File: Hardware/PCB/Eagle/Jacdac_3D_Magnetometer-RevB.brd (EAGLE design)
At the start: 25 x 25 mm, 31 parts, among them J2 SWD-ADAPTER-, J3 5V, J4 DATA, J5 GND, J6 GND, U1 STM32G030F6P6, U2 NCP114ASN330T1G, U3 TLV493D, U4 BAT54S,235

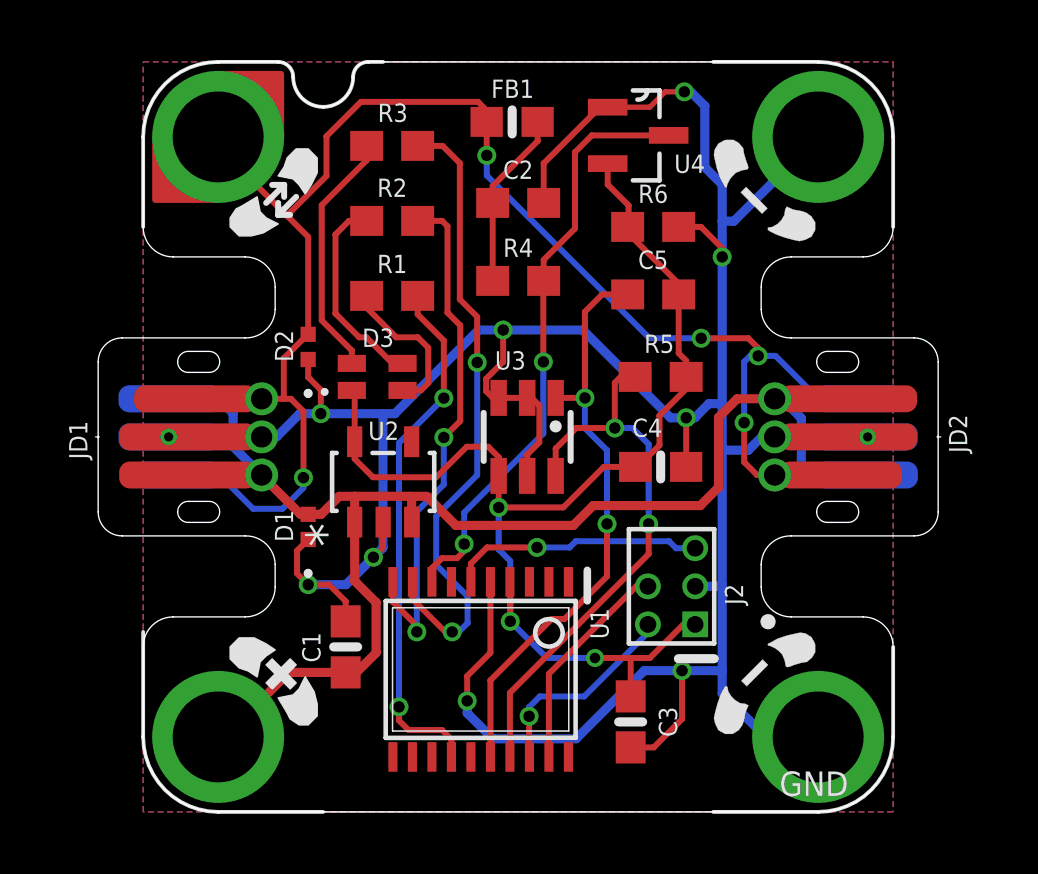
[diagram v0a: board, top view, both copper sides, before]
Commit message: Updated RevB design to match pinouts of other Jacdac modules
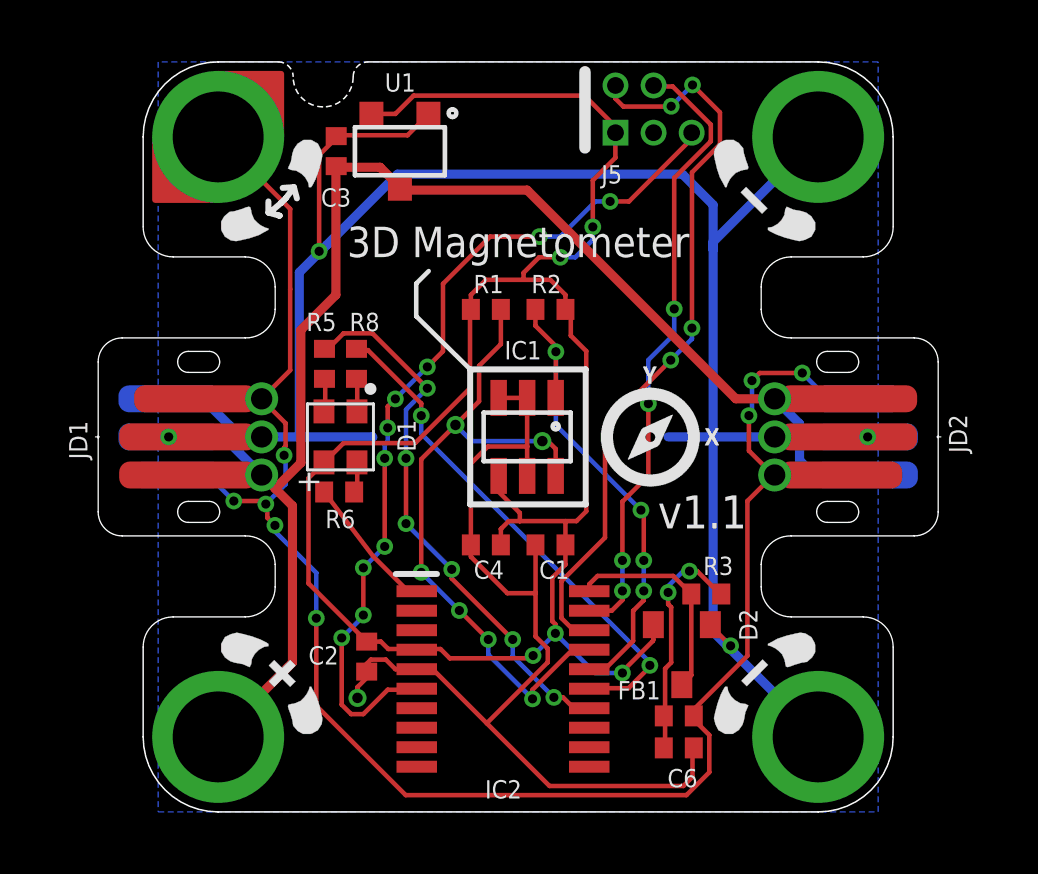
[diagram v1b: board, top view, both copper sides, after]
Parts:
- removed C5: 1uF, milador_SMD:0603
- removed D3: LED-HSMF-C114, milador_SMD:DIOSC160X150X35-4N
- removed J6: GND, milador:M3-HOLE-GND
- removed LABEL_JACDAC_PS: MILADOR-JACDAC-DEVICE-MAGNETOMETER, milador:JACDAC-3D-MAGNETOMETER
- removed LABEL_MILADOR: MILADOR-LOGO-, milador:MILADOR_LOGO1
- removed LABEL_QR_CODE: MILADOR-QR-CODE-JACDAC-MAGNETOMETER, milador:MILADOR_QR_JACDAC_MAGNETOMETER
- removed MMC_LOGO: MMC_LOGO-XSM, MMC Eagle:MMC_X-SMALL_LOGO
- removed R4: 220, milador_SMD:0603
- removed U2: NCP114ASN330T1G, milador_SMD:TSOP-5_ONS
- removed U4: BAT54S,235, milador_SMD:SOT23-3
- added C6: 33pF, milador_SMD:0402
- added IC2: STM32G030F6P6, milador_SMD:SOP65P640X120-20N
- added J1: JD, milador:M3-HOLE-DATA
- added LABEL_DEVICE: MILADOR-JACDAC-DEVICE-MAGNETOMETER, milador:JACDAC-3D-MAGNETOMETER
- added LABEL_ICON: MILADOR-ICON-MAG, milador:MILADOR_ICON_MAGNETOMETER
- added LABEL_LOGO1: MILADOR-LOGO-SM, milador:MILADOR_LOGO2
- added LABEL_LOGO2: MMC_LOGO-XSM, MMC Eagle:MMC_X-SMALL_LOGO
- added LABEL_QRCODE: MILADOR-QR-CODE-JACDAC-MAGNETOMETER, milador:MILADOR_QR_JACDAC_MAGNETOMETER
- added R8: 150R, milador_SMD:0402
- C1: value 1uF -> 0.1uF; device milador_SMD:0603-NO -> milador_SMD:0402
- C2: value 33pF -> 4.7uF; device milador_SMD:0603 -> milador_SMD:0402
- C3: value 1uF -> 4.7uF; device milador_SMD:0603-NO -> milador_SMD:0402
- C4: device milador_SMD:0603-NO -> milador_SMD:0402
- D1: value DIODE-ZENER-AA-RCLAMP0521PATCT -> C108793; device milador_SMD:DIODE-ZENER-0402 -> milador_SMD:LED-RGB-2121
- D2: value DIODE-ZENER-AA-RCLAMP0521PATCT -> BAT54S-23-3; device milador_SMD:DIODE-ZENER-0402 -> milador_SMD:SOT23-3
- FB1: value 800mA 1kR -> 1k@100MHz; device milador_SMD:0603-NO -> milador_SMD:0402
- J2: value SWD-ADAPTER- -> PWR; device milador:SWD-ADAPTER -> milador:M3-HOLE-PWR
- J3: value 5V -> GND; device milador:M3-HOLE-PWR-OUTL -> milador:M3-HOLE-GND
- J4: value DATA -> GND; device milador:M3-HOLE-DATA-NOTCH -> milador:M3-HOLE-GND
- J5: value GND -> HACK-CONNECT-5; device milador:M3-HOLE-GND -> milador:HC5-22-62
- R1, R2: value 30 -> 10k; device milador_SMD:0603 -> milador_SMD:0402
- R3: value 150 -> 220R; device milador_SMD:0603 -> milador_SMD:0402
- R5: value 4.7K -> 220R; device milador_SMD:0603 -> milador_SMD:0402
- R6: value 4.7K -> 470R; device milador_SMD:0603 -> milador_SMD:0402
- U1: value STM32G030F6P6 -> XC6206; device milador_SMD:TSSOP20 -> milador_SMD:SOT23-3-W
- moved C3 21.4 mm to (7.93, 22.0), turned to 90 degrees
- moved FB1 20.6 mm to (19.4, 3.20), turned to 0 degrees
- moved J3 20.0 mm to (24.0, 2.50)
- moved J4 20.0 mm to (24.0, 22.5), turned to 90 degrees
- moved R3 18.2 mm to (20.3, 7.26)
- moved U1 17.5 mm to (10.1, 22.0), turned to 90 degrees
- moved J2 16.3 mm to (4.00, 2.50), turned to 0 degrees
- moved D2 16.1 mm to (19.5, 5.24)
- moved C2 15.9 mm to (8.95, 5.18), turned to 270 degrees
- moved R6 12.4 mm to (8.03, 10.7)
- moved R5 11.2 mm to (7.54, 14.9), turned to 270 degrees
- moved C1 7.63 mm to (15.1, 8.90), turned to 180 degrees
- moved J5 6.76 mm to (17.2, 22.6), turned to 0 degrees
- moved C4 6.38 mm to (12.9, 8.90), turned to 180 degrees
- moved LABEL_TLV493D 6.05 mm to (14.0, 16.8)
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- renumbered U3 to IC1
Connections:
- removed net +3V3: C3.1, C4.1, C5.1, D3.1, IC1.4, J2.1, R5.2, R6.2, U1.4, U2.5, U4.2
- removed net JD_DATA: R4.2, U1.8, U4.3
- removed net J_DATA: D2.2, FB1.2, J4.H, JD1.1, JD1.6, JD1.P$3, JD2.1, JD2.6, JD2.P$3
- removed net RGB_B: R1.2, U1.14
- removed net RGB_G: R2.2, U1.10
- removed net RGB_R: R3.2, U1.9
- new net INT: IC2.3
- new net JD: D2.3, IC2.20, R3.1
- new net JD5V: C3.1, J2.H, JD1.3, JD1.4, JD1.P$1, JD2.3, JD2.4, JD2.P$1, U1.3
- new net JDF: FB1.2, J1.H, JD1.1, JD1.6, JD1.P$3, JD2.1, JD2.6, JD2.P$3
- new net LED_B: IC2.1, R6.1
- new net LED_G: IC2.14, R5.1
- new net LED_R: IC2.15, R8.1
- new net MISO: IC2.13
- new net PWM: IC2.11
- new net RST: IC2.7
- new net RX/CS: IC2.10
- new net SCK: IC2.8
- new net TX/MOSI: IC2.9
- net GND: now also C6.2, IC2.5, J3.H, J4.H, J5.3, U1.1; no longer C5.2, D1.1, J2.3, J5.H, J6.H, U1.5, U2.2, U4.1
- net N$1: now also C6.1, FB1.1, R3.2; no longer D3.4, R1.1
- net N$2: now also D1.B-, R6.2; no longer D3.3, R2.1
- net N$3: now also D1.R-, R8.2; no longer D3.2, R3.1
- net N$4: now also D1.G-, R5.2; no longer C2.1, FB1.1, R4.1
- net RESET: now also IC2.6, J5.5; no longer J2.5, U1.6
- net SCL: now also IC2.16, R2.1; no longer R6.1, U1.16
- net SDA: now also IC2.17, R1.1; no longer R5.1, U1.17
- net SWCLK: now also IC2.19, J5.4; no longer J2.4, U1.19
- net SWDIO: now also IC2.18, J5.2; no longer J2.2, U1.18
- net VCC: now also C2.1, C4.1, D1.PLUS, D2.2, IC1.4, IC2.4, J5.1, R1.2, R2.2, U1.2; no longer D1.2, J3.H, JD1.3, JD1.4, JD1.P$1, JD2.3, JD2.4, JD2.P$1, U2.1, U2.3
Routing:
- net JDF: track 0.00 -> 58.5 mm, vias 0 -> 8
- net JD5V: track 0.00 -> 53.8 mm
- net J_DATA: track 51.4 -> 0.00 mm, vias 5 -> 0
- net +3V3: track 40.4 -> 0.00 mm, vias 3 -> 0
- net RGB_R: track 21.2 -> 0.00 mm, vias 2 -> 0
- net RESET: track 8.49 -> 28.9 mm, vias 1 -> 10
- net JD_DATA: track 19.9 -> 0.00 mm, vias 2 -> 0
- net LED_G: track 0.00 -> 18.4 mm, vias 0 -> 6
- net SWDIO: track 6.93 -> 24.9 mm, vias 1 -> 4
- net RGB_B: track 17.7 -> 0.00 mm, vias 2 -> 0
- net RGB_G: track 17.4 -> 0.00 mm, vias 2 -> 0
- net LED_R: track 0.00 -> 17.2 mm, vias 0 -> 2
- net VCC: track 48.9 -> 64.1 mm, vias 0 -> 5
- net SWCLK: track 7.28 -> 20.8 mm, vias 0 -> 4
- net N$3: track 8.29 -> 1.11 mm
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- removed copper zone on layer 1, net GND
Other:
- board text added: "3D Magnetometer"
- board text added: "v1.1"
- board text removed: "GND"
- board text removed: "V1.0"

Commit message: Updated components value
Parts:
- C1, C4: value 0.1uF -> 100nF
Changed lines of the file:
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@@
 <attribute name="VALUE" x="14.4412" y="15.345" size="0.8128" layer="27" ratio="10"/>
 </element>
-<element name="C1" library="milador_SMD" library_urn="urn:adsk.eagle:library:27847482" package="0402" package3d_urn="urn:adsk.eagle:package:36491935/2" value="0.1uF" x="15.0762" y="8.9" smashed="yes" rot="R180">
+<element name="C1" library="milador_SMD" library_urn="urn:adsk.eagle:library:27847482" package="0402" package3d_urn="urn:adsk.eagle:package:36491935/2" value="100nF" x="15.0762" y="8.9" smashed="yes" rot="R180">
 <attribute name="NAME" x="14.7" y="7.77" size="0.6096" layer="25" font="vector" ratio="20"/>
 <attribute name="VALUE" x="15.7112" y="10.305" size="0.8128" layer="27" ratio="10" rot="R180"/>
 </element>
-<element name="C4" library="milador_SMD" library_urn="urn:adsk.eagle:library:27847482" package="0402" package3d_urn="urn:adsk.eagle:package:36491935/2" value="0.1uF" x="12.9238" y="8.9" smashed="yes" rot="R180">
+<element name="C4" library="milador_SMD" library_urn="urn:adsk.eagle:library:27847482" package="0402" package3d_urn="urn:adsk.eagle:package:36491935/2" value="100nF" x="12.9238" y="8.9" smashed="yes" rot="R180">
 <attribute name="NAME" x="12.5188" y="7.77" size="0.6096" layer="25" font="vector" ratio="20"/>
 <attribute name="VALUE" x="13.5588" y="10.305" size="0.8128" layer="27" ratio="10" rot="R180"/>

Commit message: Updated Magnetometer icon
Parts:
- moved LABEL_ICON 1.10 mm to (18.3, 13.6)
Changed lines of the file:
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@@
 <layer number="19" name="Unrouted" color="6" fill="1" visible="yes" active="yes"/>
 <layer number="20" name="Dimension" color="11" fill="1" visible="yes" active="yes"/>
-<layer number="21" name="tPlace" color="7" fill="1" visible="no" active="yes"/>
-<layer number="22" name="bPlace" color="7" fill="1" visible="no" active="yes"/>
+<layer number="21" name="tPlace" color="7" fill="1" visible="yes" active="yes"/>
+<layer number="22" name="bPlace" color="7" fill="1" visible="yes" active="yes"/>
 <layer number="23" name="tOrigins" color="15" fill="1" visible="yes" active="yes"/>
 <layer number="24" name="bOrigins" color="15" fill="1" visible="yes" active="yes"/>
-<layer number="25" name="tNames" color="7" fill="1" visible="no" active="yes"/>
-<layer number="26" name="bNames" color="7" fill="1" visible="no" active="yes"/>
+<layer number="25" name="tNames" color="7" fill="1" visible="yes" active="yes"/>
+<layer number="26" name="bNames" color="7" fill="1" visible="yes" active="yes"/>
 <layer number="27" name="tValues" color="7" fill="1" visible="no" active="yes"/>
 <layer number="28" name="bValues" color="7" fill="1" visible="no" active="yes"/>
@@
 </layers>
 <board>
-<fusionsync huburn="a.cGVyc29uYWw6dWUyYWQxOTI2" projecturn="a.cGVyc29uYWw6dWUyYWQxOTI2IzIwMjIwNzA2NTM3OTQ3MDMx" f3durn="urn:adsk.wipprod:dm.lineage:tg6RshVFQ_eVgbOz5fKqMA" pcbguid="" lastpulledtime="" lastsyncedchangeguid="" latestrevisionid="c85c1f68-8bb4-46bb-b6c8-edd736532134" lastsyncedrevisionid="c85c1f68-8bb4-46bb-b6c8-edd736532134" lastboardhashguid="3cf0972b-a586-93a1-9dfc-d49382ca4a7b" lastpushedtime="2022-07-13T06:56:19Z" linktopcb3d="true"/>
+<fusionsync huburn="a.cGVyc29uYWw6dWUyYWQxOTI2" projecturn="a.cGVyc29uYWw6dWUyYWQxOTI2IzIwMjIwNzA2NTM3OTQ3MDMx" f3durn="urn:adsk.wipprod:dm.lineage:tg6RshVFQ_eVgbOz5fKqMA" pcbguid="" lastpulledtime="" lastsyncedchangeguid="" latestrevisionid="bc4bedf3-121a-4f04-aa99-d77395104366" lastsyncedrevisionid="bc4bedf3-121a-4f04-aa99-d77395104366" lastboardhashguid="45f2b9e4-896e-1f0b-d066-4e348af00b0e" lastpushedtime="2022-07-16T00:10:26Z" linktopcb3d="true"/>
 <plain>
 <text x="14" y="19" size="1.016" layer="21" font="vector" ratio="13" align="center">3D Magnetometer</text>
@@
 <attribute name="VALUE" x="12.649" y="13.135" size="0.4064" layer="27" ratio="10" rot="R180"/>
 </element>
-<element name="LABEL_ICON" library="milador" library_urn="urn:adsk.eagle:library:12595918" package="MILADOR_ICON_MAGNETOMETER" package3d_urn="urn:adsk.eagle:package:36505533/1" value="MILADOR-ICON-MAG" x="18.4" y="12.5" smashed="yes"/>
+<element name="LABEL_ICON" library="milador" library_urn="urn:adsk.eagle:library:12595918" package="MILADOR_ICON_MAGNETOMETER" package3d_urn="urn:adsk.eagle:package:36505533/2" value="MILADOR-ICON-MAG" x="18.3" y="13.6" smashed="yes"/>
 </elements>
 <signals>
